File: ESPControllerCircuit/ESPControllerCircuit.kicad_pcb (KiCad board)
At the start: 2 copper layers, 75 x 30 mm, 25 parts, among them J1 Input, J2 Input, J3 Input, J4 Input, J5 Optional, U1 WeMos_mini, U2 HMHA2801, U3 PCF8574AT/3

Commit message: Change to PCF8574 model
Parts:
- U3: value PCF8574AT/3 -> PCF8574T/3,518
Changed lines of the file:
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@@
       (effects (font (size 1 1) (thickness 0.15)))
     )
-    (fp_text value PCF8574AT/3 (at 6.5 -0.25) (layer F.SilkS)
+    (fp_text value PCF8574T/3,518 (at 6.5 -0.25) (layer F.SilkS)
       (effects (font (size 1 1) (thickness 0.15)))
     )

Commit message: full_jlcpcb_assembly
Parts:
- U2: value HMHA2801 -> HMHA2801AR2; footprint Housings_SSOP:SOP-4_4.4x2.8mm_Pitch1.27mm -> Package_SO:SOIC-4_4.55x2.6mm_P1.27mm
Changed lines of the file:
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@@
-(kicad_pcb (version 20171130) (host pcbnew "(5.1.0)-1")
+(kicad_pcb (version 20171130) (host pcbnew 5.1.5-52549c5~84~ubuntu18.04.1)
   (general
     (thickness 1.6)
@@
     (add_net SDA)
   )
+  (module Package_SO:SOIC-4_4.55x2.6mm_P1.27mm (layer F.Cu)
+    (at 129.75 127.5 270)
+    (descr "SOIC, 4 Pin (https://toshiba.semicon-storage.com/info/docget.jsp?did=12884&prodName=TLP291), generated with kicad-footprint-generator ipc_gullwing_generator.py")
+    (tags "SOIC SO")
+    (attr smd)
+    (fp_text reference U2 (at 0 0.5 270) (layer F.SilkS)
+      (effects (font (size 1 1) (thickness 0.15)))
+    )
+    (fp_text value HMHA2801AR2 (at 0 2.25 270) (layer F.Fab)
+      (effects (font (size 1 1) (thickness 0.15)))
+    )
+    (fp_text user %R (at -0.25 -0.75 270) (layer F.Fab)
+      (effects (font (size 0.8 0.8) (thickness 0.15)))
+    )
+    (fp_line (start 4.3 -1.55) (end -4.3 -1.55) (layer F.CrtYd) (width 0.05))
+    (fp_line (start 4.3 1.55) (end 4.3 -1.55) (layer F.CrtYd) (width 0.05))
+    (fp_line (start -4.3 1.55) (end 4.3 1.55) (layer F.CrtYd) (width 0.05))
+    (fp_line (start -4.3 -1.55) (end -4.3 1.55) (layer F.CrtYd) (width 0.05))
+    (fp_line (start -2.275 -0.65) (end -1.625 -1.3) (layer F.Fab) (width 0.1))
+    (fp_line (start -2.275 1.3) (end -2.275 -0.65) (layer F.Fab) (width 0.1))
+    (fp_line (start 2.275 1.3) (end -2.275 1.3) (layer F.Fab) (width 0.1))
+    (fp_line (start 2.275 -1.3) (end 2.275 1.3) (layer F.Fab) (width 0.1))
+    (fp_line (start -1.625 -1.3) (end 2.275 -1.3) (layer F.Fab) (width 0.1))
+    (fp_line (start -2.385 -1.17) (end -4.05 -1.17) (layer F.SilkS) (width 0.12))
+    (fp_line (start -2.385 -1.41) (end -2.385 -1.17) (layer F.SilkS) (width 0.12))
+    (fp_line (start 0 -1.41) (end -2.385 -1.41) (layer F.SilkS) (width 0.12))
+    (fp_line (start 2.385 -1.41) (end 2.385 -1.17) (layer F.SilkS) (width 0.12))
+    (fp_line (start 0 -1.41) (end 2.385 -1.41) (layer F.SilkS) (width 0.12))
+    (fp_line (start -2.385 1.41) (end -2.385 1.17) (layer F.SilkS) (width 0.12))
+    (fp_line (start 0 1.41) (end -2.385 1.41) (layer F.SilkS) (width 0.12))
+    (fp_line (start 2.385 1.41) (end 2.385 1.17) (layer F.SilkS) (width 0.12))
+    (fp_line (start 0 1.41) (end 2.385 1.41) (layer F.SilkS) (width 0.12))
+    (pad 4 smd roundrect (at 3.25 -0.635 270) (size 1.6 0.55) (layers F.Cu F.Paste F.Mask) (roundrect_rratio 0.25)
+      (net 10 "Net-(TX1-Pad2)"))
+    (pad 3 smd roundrect (at 3.25 0.635 270) (size 1.6 0.55) (layers F.Cu F.Paste F.Mask) (roundrect_rratio 0.25)
+      (net 9 "Net-(TX1-Pad1)"))
+    (pad 2 smd roundrect (at -3.25 0.635 270) (size 1.6 0.55) (layers F.Cu F.Paste F.Mask) (roundrect_rratio 0.25)
+      (net 1 GND))
+    (pad 1 smd roundrect (at -3.25 -0.635 270) (size 1.6 0.55) (layers F.Cu F.Paste F.Mask) (roundrect_rratio 0.25)
+      (net 7 "Net-(R3-Pad1)"))
+    (model ${KISYS3DMOD}/Package_SO.3dshapes/SOIC-4_4.55x2.6mm_P1.27mm.wrl
+      (at (xyz 0 0 0))
+      (scale (xyz 1 1 1))
+      (rotate (xyz 0 0 0))
+    )
+  )
   (module SMD_Packages:SO-16-W (layer F.Cu)
     (at 132.25 113 270)
@@
       (at (xyz 0 0 0))
       (scale (xyz 1 1 1))
-      (rotate (xyz 0 0 0))
-    )
-  )
-  (module Housings_SSOP:SOP-4_4.4x2.8mm_Pitch1.27mm (layer F.Cu)
-    (at 129.75 127.5 270)
-    (descr "4-Lead Plastic Small Outline http://www.vishay.com/docs/49633/sg2098.pdf")
-    (tags "SOP 1.27")
-    (attr smd)
-    (fp_text reference U2 (at 0 0.5 270) (layer F.SilkS)
-      (effects (font (size 1 1) (thickness 0.15)))
-    )
-    (fp_text value HMHA2801 (at 0 2.25 270) (layer F.Fab)
-      (effects (font (size 1 1) (thickness 0.15)))
-    )
-    (fp_text user %R (at -0.25 -0.75 270) (layer F.Fab)
-      (effects (font (size 0.8 0.8) (thickness 0.15)))
-    )
-    (fp_line (start -2.2 -0.79) (end -1.6 -1.39) (layer F.Fab) (width 0.1))
-    (fp_line (start -2.4 -1.59) (end -2.4 -1.19) (layer F.SilkS) (width 0.12))
-    (fp_line (start -2.4 -1.19) (end -3.8 -1.19) (layer F.SilkS) (width 0.12))
-    (fp_line (start -1.6 -1.39) (end 2.2 -1.39) (layer F.Fab) (width 0.1))
-    (fp_line (start 2.2 -1.39) (end 2.2 1.41) (layer F.Fab) (width 0.1))
-    (fp_line (start 2.2 1.41) (end -2.2 1.41) (layer F.Fab) (width 0.1))
-    (fp_line (start -2.2 1.41) (end -2.2 -0.79) (layer F.Fab) (width 0.1))
-    (fp_line (start -2.4 -1.59) (end 2.4 -1.59) (layer F.SilkS) (width 0.12))
-    (fp_line (start -2.4 1.61) (end 2.4 1.61) (layer F.SilkS) (width 0.12))
-    (fp_line (start -4.05 -1.64) (end 4.05 -1.64) (layer F.CrtYd) (width 0.05))
-    (fp_line (start -4.05 -1.64) (end -4.05 1.66) (layer F.CrtYd) (width 0.05))
-    (fp_line (start 4.05 1.66) (end 4.05 -1.64) (layer F.CrtYd) (width 0.05))
-    (fp_line (start 4.05 1.66) (end -4.05 1.66) (layer F.CrtYd) (width 0.05))
-    (pad 1 smd rect (at -3.15 -0.64 270) (size 1.3 0.8) (layers F.Cu F.Paste F.Mask)
-      (net 7 "Net-(R3-Pad1)"))
-    (pad 2 smd rect (at -3.15 0.64 270) (size 1.3 0.8) (layers F.Cu F.Paste F.Mask)
-      (net 1 GND))
-    (pad 3 smd rect (at 3.15 0.64 270) (size 1.3 0.8) (layers F.Cu F.Paste F.Mask)
-      (net 9 "Net-(TX1-Pad1)"))
-    (pad 4 smd rect (at 3.15 -0.64 270) (size 1.3 0.8) (layers F.Cu F.Paste F.Mask)
-      (net 10 "Net-(TX1-Pad2)"))
-    (model ${KISYS3DMOD}/Housings_SSOP.3dshapes/SOP-4_4.4x2.8mm_Pitch1.27mm.wrl
-      (at (xyz 0 0 0))
-      (scale (xyz 1 1 1))

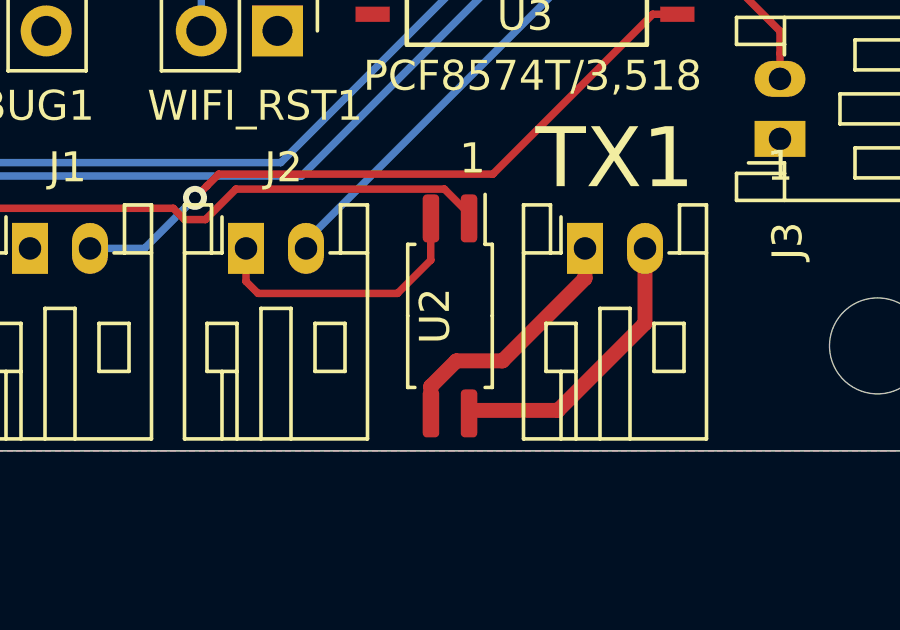
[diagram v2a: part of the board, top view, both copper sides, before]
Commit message: Replace HMHA2801AR2 by EL3H7(B)(TA)-G
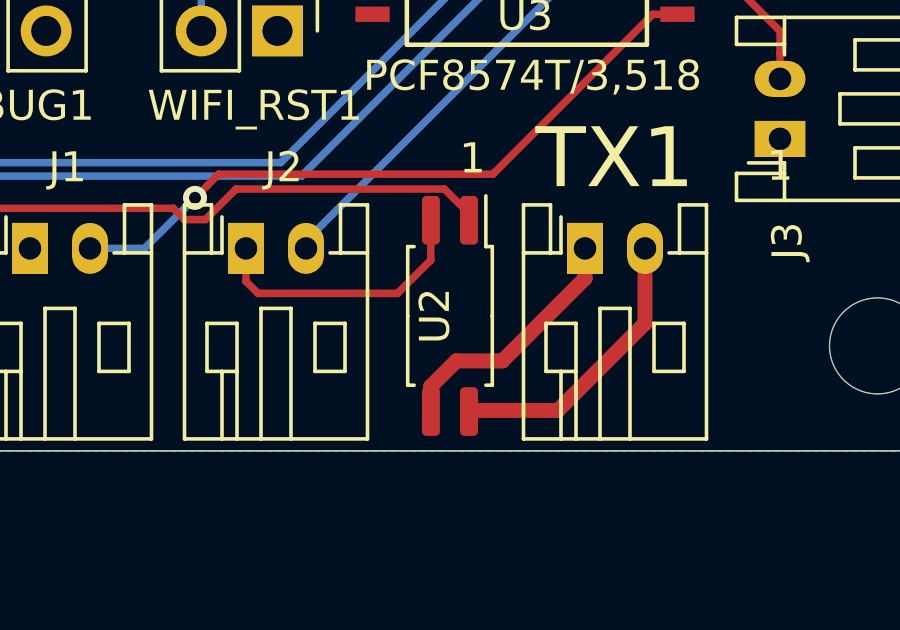
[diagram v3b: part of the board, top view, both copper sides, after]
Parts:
- U2: value HMHA2801AR2 -> EL3H7(B)(TA)-G; footprint Package_SO:SOIC-4_4.55x2.6mm_P1.27mm -> Package_SO:SOP-4_4.4x2.6mm_P1.27mm
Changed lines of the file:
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@@
     (add_net SDA)
   )
-  (module Package_SO:SOIC-4_4.55x2.6mm_P1.27mm (layer F.Cu)
+  (module Package_SO:SOP-4_4.4x2.6mm_P1.27mm (layer F.Cu)
     (at 129.75 127.5 270)
-    (descr "SOIC, 4 Pin (https://toshiba.semicon-storage.com/info/docget.jsp?did=12884&prodName=TLP291), generated with kicad-footprint-generator ipc_gullwing_generator.py")
-    (tags "SOIC SO")
+    (descr "SOP, 4 Pin (http://www.vishay.com/docs/83510/tcmt1100.pdf), generated with kicad-footprint-generator ipc_gullwing_generator.py")
+    (tags "SOP SO")
     (attr smd)
     (fp_text reference U2 (at 0 0.5 270) (layer F.SilkS)
       (effects (font (size 1 1) (thickness 0.15)))
     )
-    (fp_text value HMHA2801AR2 (at 0 2.25 270) (layer F.Fab)
+    (fp_text value "EL3H7(B)(TA)-G" (at 0 2.25 270) (layer F.Fab)
       (effects (font (size 1 1) (thickness 0.15)))
     )
@@
       (effects (font (size 0.8 0.8) (thickness 0.15)))
     )
-    (fp_line (start 4.3 -1.55) (end -4.3 -1.55) (layer F.CrtYd) (width 0.05))
-    (fp_line (start 4.3 1.55) (end 4.3 -1.55) (layer F.CrtYd) (width 0.05))
-    (fp_line (start -4.3 1.55) (end 4.3 1.55) (layer F.CrtYd) (width 0.05))
-    (fp_line (start -4.3 -1.55) (end -4.3 1.55) (layer F.CrtYd) (width 0.05))
-    (fp_line (start -2.275 -0.65) (end -1.625 -1.3) (layer F.Fab) (width 0.1))
-    (fp_line (start -2.275 1.3) (end -2.275 -0.65) (layer F.Fab) (width 0.1))
-    (fp_line (start 2.275 1.3) (end -2.275 1.3) (layer F.Fab) (width 0.1))
-    (fp_line (start 2.275 -1.3) (end 2.275 1.3) (layer F.Fab) (width 0.1))
-    (fp_line (start -1.625 -1.3) (end 2.275 -1.3) (layer F.Fab) (width 0.1))
-    (fp_line (start -2.385 -1.17) (end -4.05 -1.17) (layer F.SilkS) (width 0.12))
-    (fp_line (start -2.385 -1.41) (end -2.385 -1.17) (layer F.SilkS) (width 0.12))
-    (fp_line (start 0 -1.41) (end -2.385 -1.41) (layer F.SilkS) (width 0.12))
-    (fp_line (start 2.385 -1.41) (end 2.385 -1.17) (layer F.SilkS) (width 0.12))
-    (fp_line (start 0 -1.41) (end 2.385 -1.41) (layer F.SilkS) (width 0.12))
-    (fp_line (start -2.385 1.41) (end -2.385 1.17) (layer F.SilkS) (width 0.12))
-    (fp_line (start 0 1.41) (end -2.385 1.41) (layer F.SilkS) (width 0.12))
-    (fp_line (start 2.385 1.41) (end 2.385 1.17) (layer F.SilkS) (width 0.12))
-    (fp_line (start 0 1.41) (end 2.385 1.41) (layer F.SilkS) (width 0.12))
-    (pad 4 smd roundrect (at 3.25 -0.635 270) (size 1.6 0.55) (layers F.Cu F.Paste F.Mask) (roundrect_rratio 0.25)
+    (fp_line (start 4.25 -1.55) (end -4.25 -1.55) (layer F.CrtYd) (width 0.05))
+    (fp_line (start 4.25 1.55) (end 4.25 -1.55) (layer F.CrtYd) (width 0.05))
+    (fp_line (start -4.25 1.55) (end 4.25 1.55) (layer F.CrtYd) (width 0.05))
+    (fp_line (start -4.25 -1.55) (end -4.25 1.55) (layer F.CrtYd) (width 0.05))
+    (fp_line (start -2.2 -0.65) (end -1.55 -1.3) (layer F.Fab) (width 0.1))
+    (fp_line (start -2.2 1.3) (end -2.2 -0.65) (layer F.Fab) (width 0.1))
+    (fp_line (start 2.2 1.3) (end -2.2 1.3) (layer F.Fab) (width 0.1))
+    (fp_line (start 2.2 -1.3) (end 2.2 1.3) (layer F.Fab) (width 0.1))
+    (fp_line (start -1.55 -1.3) (end 2.2 -1.3) (layer F.Fab) (width 0.1))
+    (fp_line (start -2.31 -1.195) (end -4 -1.195) (layer F.SilkS) (width 0.12))
+    (fp_line (start -2.31 -1.41) (end -2.31 -1.195) (layer F.SilkS) (width 0.12))
+    (fp_line (start 0 -1.41) (end -2.31 -1.41) (layer F.SilkS) (width 0.12))
+    (fp_line (start 2.31 -1.41) (end 2.31 -1.195) (layer F.SilkS) (width 0.12))
+    (fp_line (start 0 -1.41) (end 2.31 -1.41) (layer F.SilkS) (width 0.12))
+    (fp_line (start -2.31 1.41) (end -2.31 1.195) (layer F.SilkS) (width 0.12))
+    (fp_line (start 0 1.41) (end -2.31 1.41) (layer F.SilkS) (width 0.12))
+    (fp_line (start 2.31 1.41) (end 2.31 1.195) (layer F.SilkS) (width 0.12))
+    (fp_line (start 0 1.41) (end 2.31 1.41) (layer F.SilkS) (width 0.12))
+    (pad 4 smd roundrect (at 3.1875 -0.635 270) (size 1.625 0.6) (layers F.Cu F.Paste F.Mask) (roundrect_rratio 0.25)
       (net 10 "Net-(TX1-Pad2)"))
-    (pad 3 smd roundrect (at 3.25 0.635 270) (size 1.6 0.55) (layers F.Cu F.Paste F.Mask) (roundrect_rratio 0.25)
+    (pad 3 smd roundrect (at 3.1875 0.635 270) (size 1.625 0.6) (layers F.Cu F.Paste F.Mask) (roundrect_rratio 0.25)
       (net 9 "Net-(TX1-Pad1)"))
-    (pad 2 smd roundrect (at -3.25 0.635 270) (size 1.6 0.55) (layers F.Cu F.Paste F.Mask) (roundrect_rratio 0.25)
+    (pad 2 smd roundrect (at -3.1875 0.635 270) (size 1.625 0.6) (layers F.Cu F.Paste F.Mask) (roundrect_rratio 0.25)
       (net 1 GND))
-    (pad 1 smd roundrect (at -3.25 -0.635 270) (size 1.6 0.55) (layers F.Cu F.Paste F.Mask) (roundrect_rratio 0.25)
+    (pad 1 smd roundrect (at -3.1875 -0.635 270) (size 1.625 0.6) (layers F.Cu F.Paste F.Mask) (roundrect_rratio 0.25)
       (net 7 "Net-(R3-Pad1)"))
-    (model ${KISYS3DMOD}/Package_SO.3dshapes/SOIC-4_4.55x2.6mm_P1.27mm.wrl
+    (model ${KISYS3DMOD}/Package_SO.3dshapes/SOP-4_4.4x2.6mm_P1.27mm.wrl
       (at (xyz 0 0 0))
       (scale (xyz 1 1 1))

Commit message: Ready for use...
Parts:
- C_SEN1, J5: footprint Pin_Headers:Pin_Header_Straight_1x03_Pitch2.54mm -> Connector_PinHeader_2.54mm:PinHeader_1x03_P2.54mm_Vertical
- D1: footprint LEDs:LED_D5.0mm -> LED_THT:LED_D5.0mm
- DEBUG1, WIFI_RST1: footprint Pin_Headers:Pin_Header_Straight_1x02_Pitch2.54mm -> Connector_PinHeader_2.54mm:PinHeader_1x02_P2.54mm_Vertical
- J1, J2, J3, J4, RX1, TX1: footprint Connectors_JST:JST_PH_S2B-PH-K_02x2.00mm_Angled -> Connector_JST:JST_PH_S2B-PH-K_1x02_P2.00mm_Horizontal
- JRELAY1: footprint Pin_Headers:Pin_Header_Straight_1x06_Pitch2.54mm -> Connector_PinHeader_2.54mm:PinHeader_1x06_P2.54mm_Vertical
- R1, R2, R3, R4, R5: footprint Resistors_SMD:R_0805_HandSoldering -> Resistors_SMD:R_0805_2012Metric_Pad1.15x1.40mm_HandSolder
- U3: footprint SMD_Packages:SO-16-W -> Package_SO:SOIC-16W_7.5x10.3mm_P1.27mm
- turned U3 to 0 degrees
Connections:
- U1 pad 7: (no net) -> Net-(U1-Pad7)
- U1 pad 8: (no net) -> Net-(U1-Pad8)
- U1 pad 9: (no net) -> Net-(U1-Pad9)
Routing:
- net Net-(TX1-Pad1): track 8.43 -> 9.93 mm
- net +3V3: track 90.2 -> 91.2 mm
- net Net-(JRELAY1-Pad2): track 9.25 -> 10.3 mm
